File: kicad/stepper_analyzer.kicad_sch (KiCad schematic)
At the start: 50 parts, among them J1 Connector_Conn_01x04_Male, J2 Connector_Conn_01x04_Male, J3 Connector_Conn_01x04_Male, J4 Connector_Conn_01x04_Male, M1 Motor, M2 Motor, Q1 AO3400A, U1 ACS70331EOLCTR-2P5B3, U2 ACS70331EOLCTR-2P5B3, U3 ACS70331EOLCTR-2P5B3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

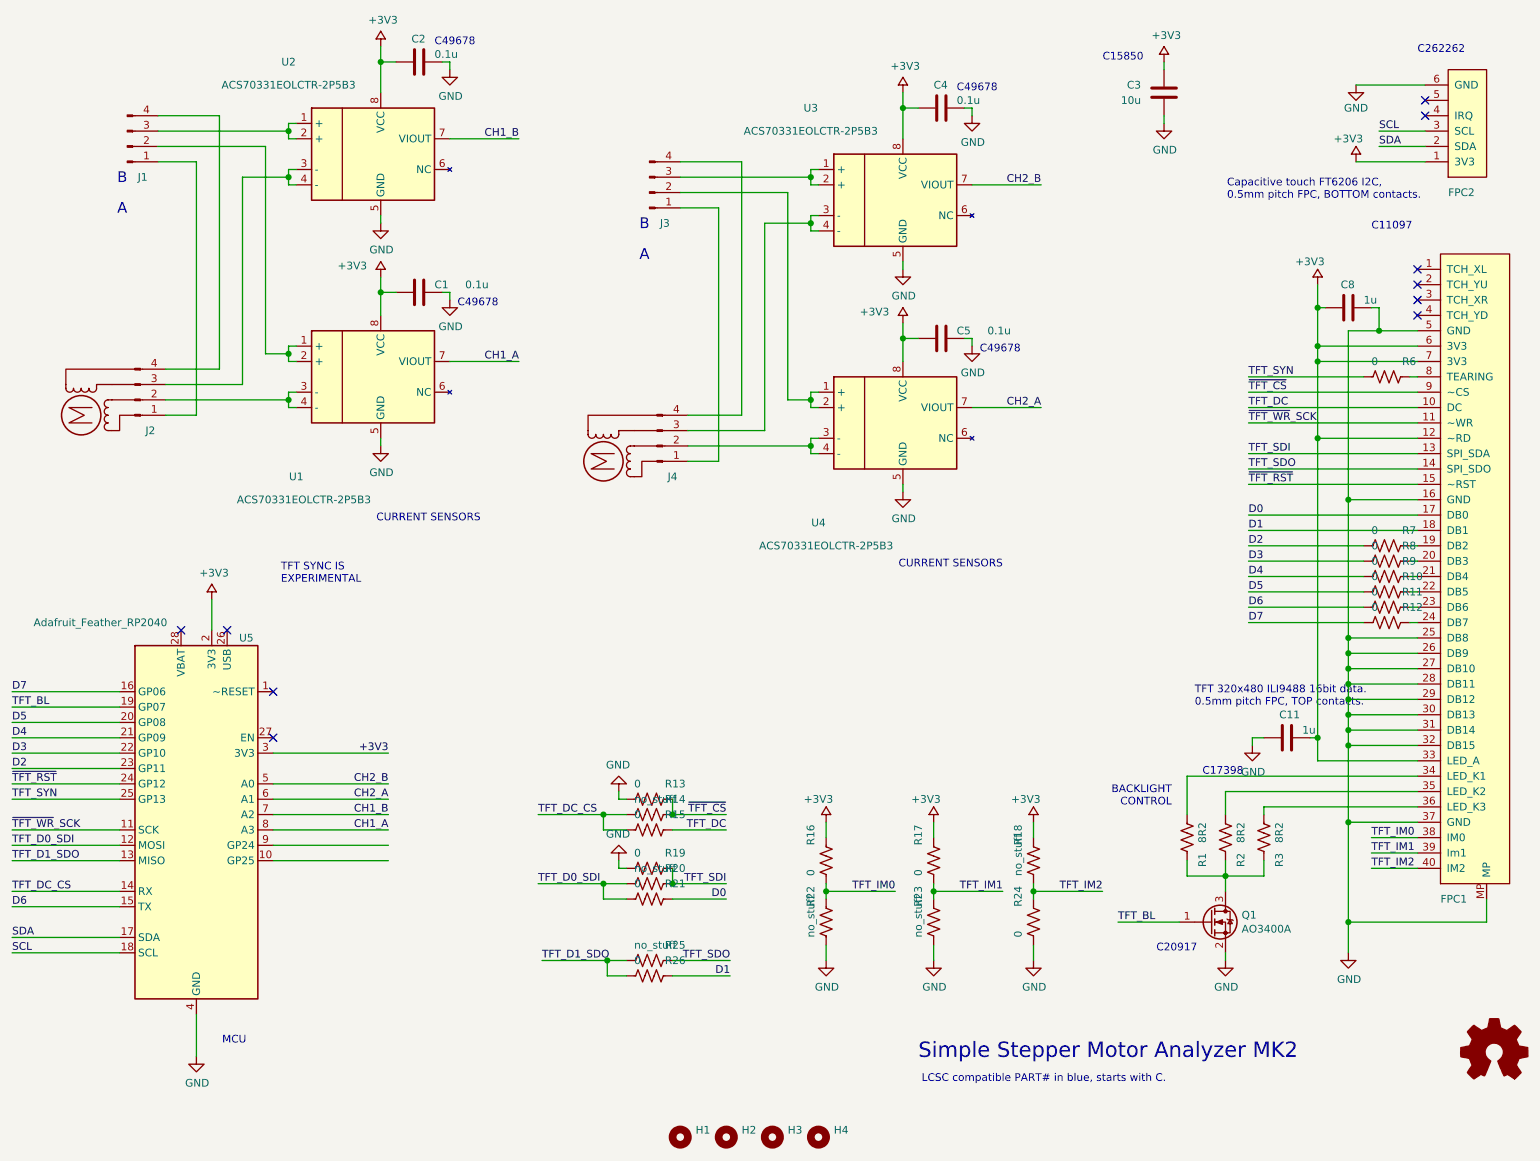
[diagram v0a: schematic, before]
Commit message: Update PCB to use TMCS1100A4QDRQ1
TMCS1100A4QDRQ1 is compatible with the old current sense device, except needs a reference voltage.
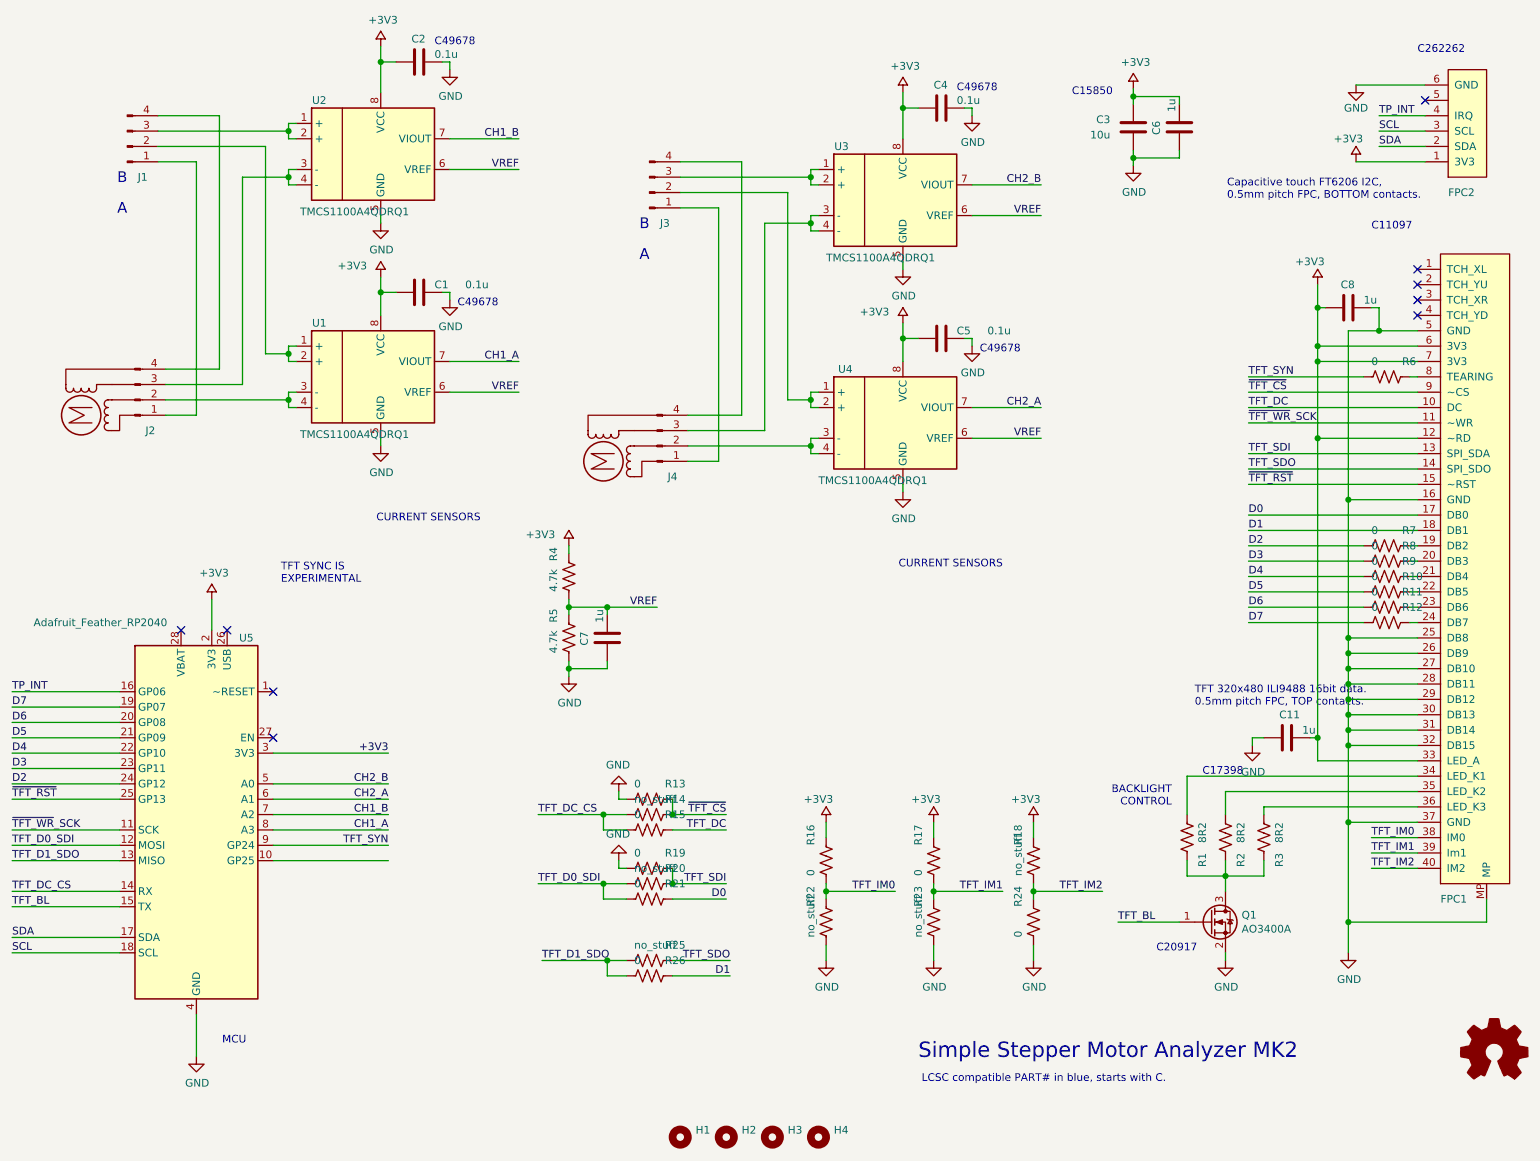
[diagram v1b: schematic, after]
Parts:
- added C6, C7: 1u, stepper_motor_analyzer:C_0805_2012Metric_Pad1.15x1.40mm_HandSolder, symbol Device:C
- added R4, R5: 4.7k, Resistor_SMD:R_0402_1005Metric_Pad0.72x0.64mm_HandSolder, symbol Device:R_US
- U1, U2, U3, U4: value ACS70331EOLCTR-2P5B3 -> TMCS1100A4QDRQ1; symbol stepper_motor_analyzer:ACS70331_soic8 -> stepper_motor_analyzer:TMCS1100
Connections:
- net +3V3: now also C6.1, R4.1
- net D2: now also U5.24 (GP12); no longer U5.23 (GP11)
- net D3: now also U5.23 (GP11); no longer U5.22 (GP10)
- net D4: now also U5.22 (GP10); no longer U5.21 (GP09)
- net D5: now also U5.21 (GP09); no longer U5.20 (GP08)
- net D6: now also U5.20 (GP08); no longer U5.15 (TX)
- net D7: now also U5.19 (GP07); no longer U5.16 (GP06)
- net GND: now also C6.2, C7.2, R5.2
- net TFT_BL: now also U5.15 (TX); no longer U5.19 (GP07)
- net TFT_SYN: now also U5.9 (GP24); no longer U5.25 (GP13)
- net ~{TFT_RST}: now also U5.25 (GP13); no longer U5.24 (GP12)
- net TP_INT: now reaches FPC2.4 (IRQ)
- net TP_INT: now also U5.16 (GP06)
- net VREF: now reaches U2.6 (VREF)
- net VREF: now also U1.6 (VREF), U3.6 (VREF), U4.6 (VREF), C7.1, R4.2, R5.1
- no-connect marks 10 -> 9
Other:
- moved on the sheet: C3
